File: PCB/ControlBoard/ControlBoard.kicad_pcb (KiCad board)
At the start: 4 copper layers, 100 x 100 mm, 115 parts, among them J1 Conn_01x05, J10 Screw_Terminal_01x03, J11 Conn_01x04, J12 USB4105-GF-A-120, J13 Screw_Terminal_01x02, J14 Screw_Terminal_01x02, J2 Conn_01x05, J4 Conn_01x10, J5 Conn_01x10, J6 Conn_01x10, J7 Conn_01x10, J8 Conn_01x14, J9 Conn_01x04, M1 Fan_4pin, M2 Fan_4pin, M3 Fan_4pin, M4 Fan_4pin, U10 TMP102xxDRL, U11 L7815, U12 MCP4728, U13 L7805, U14 SD8942, U2 ADS1115IDGS, U5 74HC4051, U6 LMR33630ADDA, U7 STM32G431C6Tx, U8 USBLC6-2SC6, U9 FM24C64B, Y1 Crystal_GND24

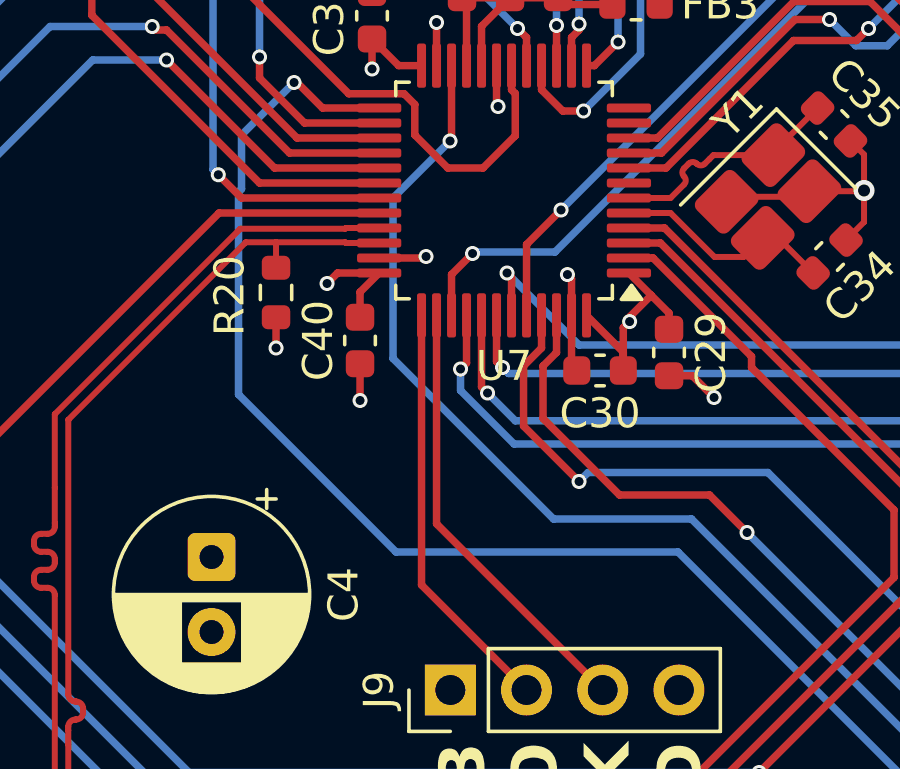
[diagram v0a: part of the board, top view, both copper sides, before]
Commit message: Fixed MCU Reset Line
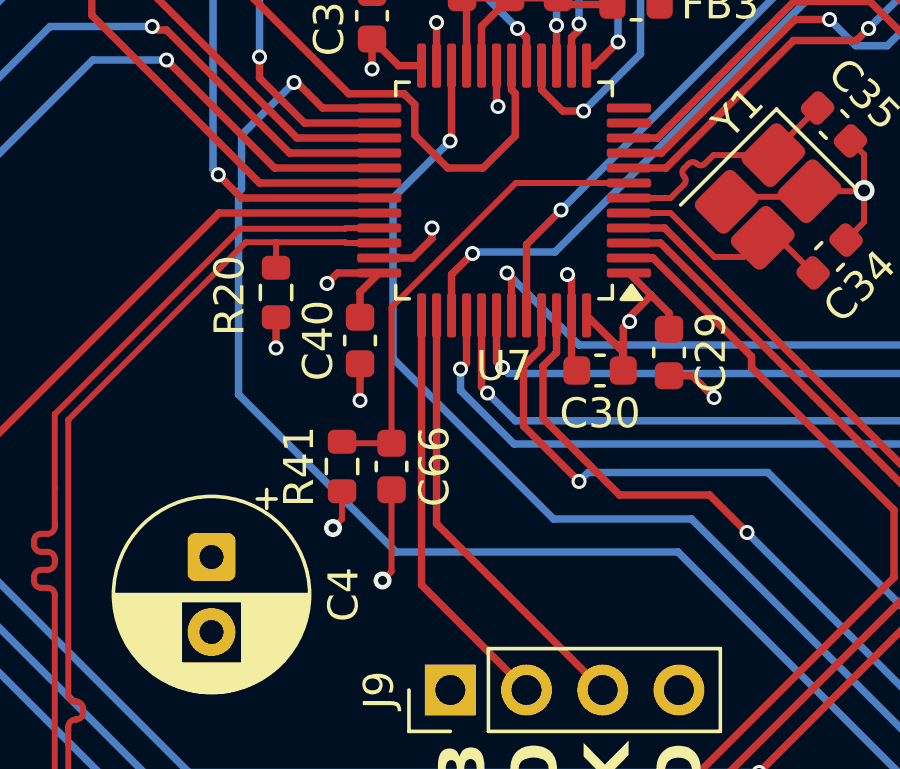
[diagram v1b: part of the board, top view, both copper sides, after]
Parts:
- added C66: 100n, Capacitor_SMD:C_0603_1608Metric, F.Cu at (123.2, 94.8)
- added R41: 10k, Resistor_SMD:R_0603_1608Metric, F.Cu at (121.6, 94.8)
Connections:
- U7 pad 7: unconnected-(U7-PG10-Pad7) -> /~{RST}
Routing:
- net /~{RST}: track 0.00 -> 15.8 mm
- net Masa: track 186.7 -> 190.6 mm, vias 63 -> 64
- net +3V3: track 48.2 -> 49.5 mm, vias 14 -> 15
